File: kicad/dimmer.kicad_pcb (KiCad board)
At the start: 2 copper layers, 60 x 60 mm, 28 parts, among them J1 FTDI, J2 AC IN, J3 Load Out, J4 LED_BYPASS, Q1 S8550 PNP, SW1 Reset, SW2 Prog, T1 Myrra_47121, U1 ESP-03, U2 MOC3021M, U3 4N25

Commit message: Add some more descriptive text
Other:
- board text added: "E"
- board text added: "L"
- board text added: "LEN"
- board text added: "N"
- board text added: "NEL"
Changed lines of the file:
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@@
     (area 118.11 66.3 180.49 129.67)
     (thickness 1.6)
-    (drawings 18)
+    (drawings 28)
     (tracks 189)
     (zones 0)
@@
   )
   (layers
-    (0 F.Cu signal)
-    (31 B.Cu signal)
+    (0 F.Cu signal hide)
+    (31 B.Cu signal hide)
     (32 B.Adhes user)
     (33 F.Adhes user)
@@
     )
   )
-  (gr_text "kiall.macinnes.ie/p/esp8266-dimmer\nv1.0" (at 149.225 88.773) (layer B.SilkS)
+  (gr_text LEN (at 176.911 69.85) (layer F.SilkS)
+    (effects (font (size 1 1) (thickness 0.25)))
+  )
+  (gr_text NEL (at 121.412 70.231) (layer F.SilkS)
+    (effects (font (size 1 1) (thickness 0.25)))
+  )
+  (gr_text SUPPLY (at 162.941 71.501 180) (layer B.SilkS)
+    (effects (font (size 1 1) (thickness 0.25)) (justify mirror))
+  )
+  (gr_text LOAD (at 135.636 71.501 180) (layer B.SilkS)
+    (effects (font (size 1 1) (thickness 0.25)) (justify mirror))
+  )
+  (gr_text N (at 172.847 69.723) (layer B.SilkS)
+    (effects (font (size 1.5 1.5) (thickness 0.3)) (justify mirror))
+  )
+  (gr_text N (at 125.603 69.723) (layer B.SilkS)
+    (effects (font (size 1.5 1.5) (thickness 0.3)) (justify mirror))
+  )
+  (gr_text E (at 135.636 69.723) (layer B.SilkS)
+    (effects (font (size 1.5 1.5) (thickness 0.3)) (justify mirror))
+  )
+  (gr_text E (at 162.814 69.723) (layer B.SilkS)
+    (effects (font (size 1.5 1.5) (thickness 0.3)) (justify mirror))
+  )
+  (gr_text L (at 152.654 69.596 180) (layer B.SilkS)
+    (effects (font (size 1.5 1.5) (thickness 0.3)) (justify mirror))
+  )
+  (gr_text L (at 145.542 69.596 180) (layer B.SilkS)
+    (effects (font (size 1.5 1.5) (thickness 0.3)) (justify mirror))
+  )
+  (gr_text "kiall.macinnes.ie/p/esp8266-dimmer\nv1.0" (at 149.225 88.773 180) (layer B.SilkS)
     (effects (font (size 1.5 1.5) (thickness 0.3)) (justify mirror))
   )
@@
     (effects (font (size 1.5 1.5) (thickness 0.3)))
   )
-  (gr_text SUPPLY (at 177.165 74.295 90) (layer F.SilkS)
+  (gr_text SUPPLY (at 177.038 75.057 90) (layer F.SilkS)
     (effects (font (size 1.5 1.5) (thickness 0.3)))
   )

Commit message: Add HK
Someone I know has a "problem" with HK ;)
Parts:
- added G***: LOGO, tmp:Hello_Kitty, B.Cu at (128.4, 116.3)

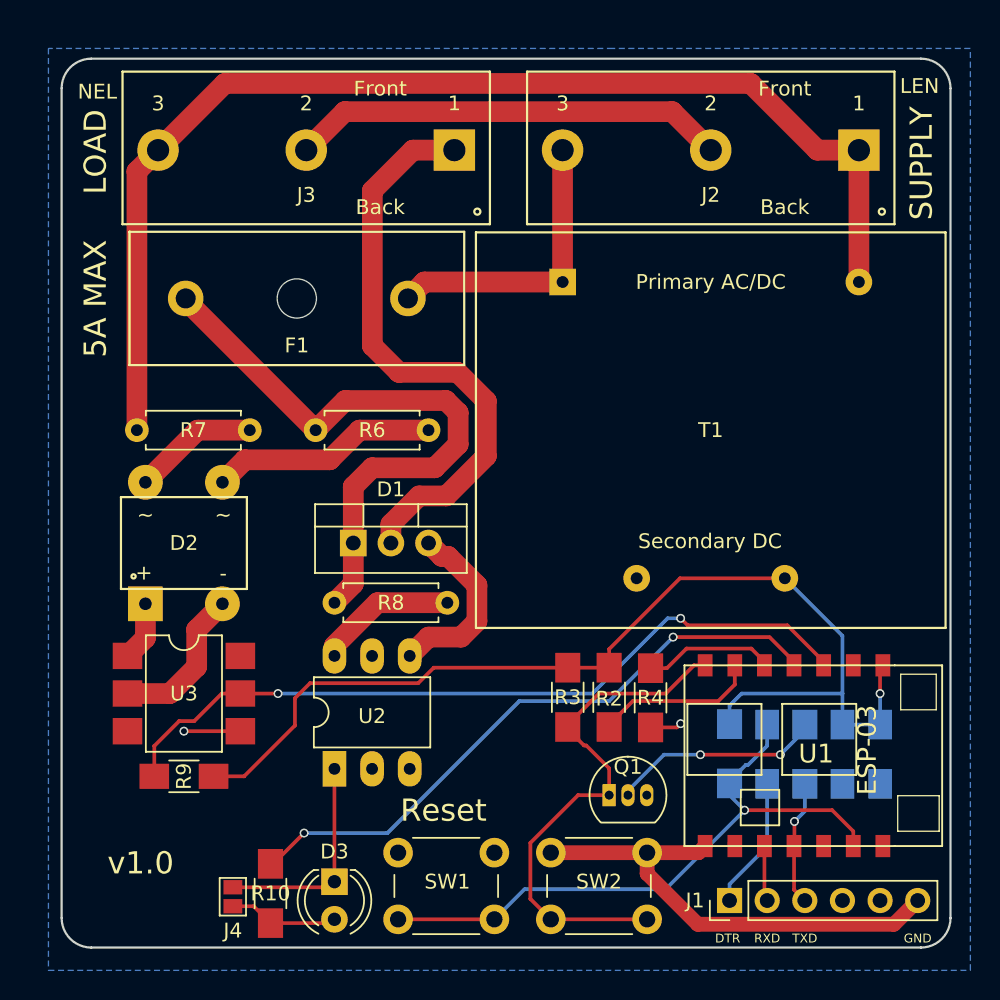
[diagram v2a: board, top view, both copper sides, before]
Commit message: Rev 1.1: Fix triac connections
Pins 1 and 2 on the triac D1 were connected in backwords, preventing
the circuit from working.
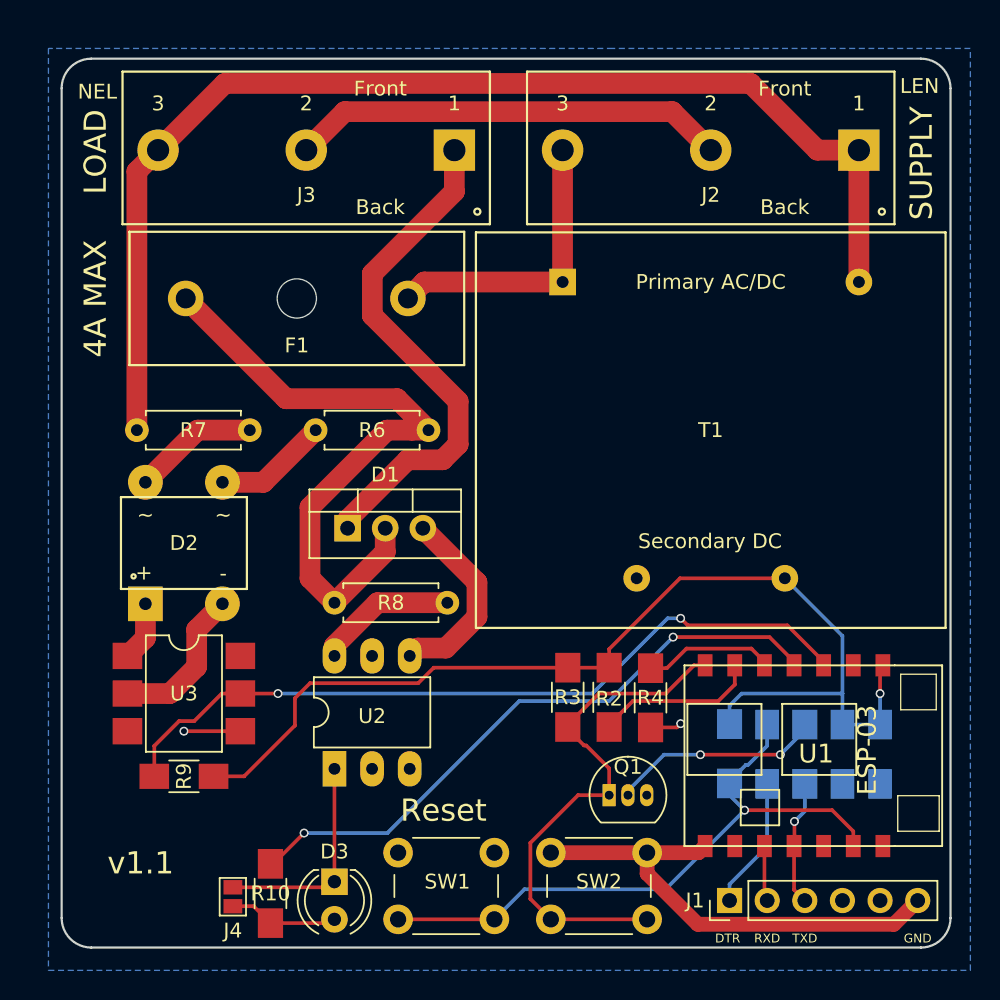
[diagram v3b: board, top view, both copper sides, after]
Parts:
- moved R6 7.62 mm to (136.1, 93.1), turned to 0 degrees
- moved D1 1.07 mm to (138.3, 99.7)
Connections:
- D1 pad 1: Net-(D1-Pad1) -> /DimmedLiveOut
- D1 pad 2: /DimmedLiveOut -> Net-(D1-Pad2)
- F1 pad 2: Net-(D1-Pad1) -> Net-(D1-Pad2)
- R6 pad 2: Net-(D1-Pad1) -> Net-(D1-Pad2)
- R8 pad 2: Net-(D1-Pad1) -> Net-(D1-Pad2)
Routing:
- net Net-(D1-Pad2): track 0.00 -> 43.9 mm
- net Net-(D1-Pad1): track 42.1 -> 0.00 mm
- net Net-(D2-Pad3): track 15.4 -> 7.75 mm
- net /DimmedLiveOut: track 39.7 -> 34.7 mm
- net Net-(D1-Pad3): track 12.4 -> 13.1 mm
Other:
- board text added: "4A MAX"
- board text added: "kiall.macinnes.ie/p/esp8266-dimmer v1.1"
- board text added: "v1.1"
- board text removed: "5A MAX"
- board text removed: "kiall.macinnes.ie/p/esp8266-dimmer v1.0"
- board text removed: "v1.0"

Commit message: Update for v1.2 - Fixes and board redesign
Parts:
- removed G***: LOGO, tmp:Hello_Kitty
- removed J4: LED_BYPASS, Connectors:GS2
- added J5: PWRIN, Pin_Headers:Pin_Header_Straight_1x02_Pitch2.54mm, F.Cu at (149.6, 111.3)
- added R11: 330, Resistors_SMD:R_1206_HandSoldering, B.Cu at (142.7, 116.6)
- C3: footprint Capacitors_SMD:C_1206_HandSoldering -> Capacitors_SMD:CP_Elec_8x10.5; moved to F.Cu
- D1: footprint TO_SOT_Packages_THT:TO-220_Vertical -> TO_SOT_Packages_THT:TO-220-3_Vertical
- R10, R2, R3, R4, R9: moved to B.Cu
- U3: footprint Housings_DIP:DIP-6_W7.62mm_SMD -> Housings_DIP:SMDIP-6_W9.53mm
- moved J2 28.5 mm to (134.4, 75.4)
- moved J3 27.3 mm to (162.8, 75.4)
- moved C3 18.0 mm to (156.2, 114.8)
- moved R5 17.0 mm to (156.2, 126.0), turned to 180 degrees
- moved SW2 13.2 mm to (139.3, 125.2), turned to 180 degrees
- moved R8 12.5 mm to (133.3, 100.3), turned to 90 degrees
- moved D3 12.2 mm to (144.8, 113.8), turned to 90 degrees
- moved R6 11.5 mm to (127.3, 100.3), turned to 90 degrees
- moved R7 11.0 mm to (123.4, 100.3), turned to 90 degrees
- moved R4 11.0 mm to (168.7, 115.8)
- moved R2 10.5 mm to (164.1, 104.4)
- moved R3 10.5 mm to (161.3, 104.4)
- moved U3 10.2 mm to (125.5, 120.9), turned to 270 degrees
- moved SW1 8.11 mm to (149.0, 125.2), turned to 180 degrees
- moved R10 8.09 mm to (135.4, 116.6), turned to 180 degrees
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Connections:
- D3 pad 2: Net-(D3-Pad2) -> +3V3
- R10 pad 2: Net-(D3-Pad2) -> Net-(R10-Pad2)
- T1 pad 1: /esp8266-base/AC+ -> /esp8266-base/AC-
- T1 pad 5: /esp8266-base/AC- -> /esp8266-base/AC+
- U2 pad 1: Net-(D3-Pad1) -> Net-(R10-Pad2)
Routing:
- net GND: track 38.3 -> 5.65 mm, vias 2 -> 3
- net /esp8266-base/AC+: track 19.8 -> 43.9 mm
- net +3V3: track 73.4 -> 96.0 mm, vias 1 -> 2
- net /DimmedLiveOut: track 34.7 -> 52.0 mm
- net Net-(D1-Pad2): track 43.9 -> 29.5 mm
- net Net-(D3-Pad1): track 14.6 -> 2.81 mm
- net Net-(Q1-Pad2): track 14.3 -> 4.36 mm, vias 2 -> 0
- net /ZeroCrossingOut: track 52.3 -> 61.0 mm, vias 2 -> 1
- net Net-(D2-Pad1): track 4.02 -> 12.7 mm
- net Net-(D1-Pad3): track 13.1 -> 5.14 mm
- net /esp8266-base/GPIO0: track 35.8 -> 43.7 mm, vias 0 -> 3
- net /DimmerIn: track 42.8 -> 35.2 mm, vias 2 -> 1
- net Net-(D3-Pad2): track 7.43 -> 0.00 mm
- net Net-(R2-Pad2): track 11.1 -> 4.07 mm, vias 0 -> 1
- net /esp8266-base/TXD: track 8.48 -> 15.0 mm, vias 1 -> 0
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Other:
- board text added: "Prog"
- board text added: "RX"
- board text added: "TX"
- board text added: "kiall.macinnes.ie/p/esp8266-dimmer v1.2"
- board text added: "v1.2"
- board text removed: "LEN"
- board text removed: "NEL"
- board text removed: "RXD"
- board text removed: "TXD"
- board text removed: "kiall.macinnes.ie/p/esp8266-dimmer v1.1"
- board text removed: "v1.1"
